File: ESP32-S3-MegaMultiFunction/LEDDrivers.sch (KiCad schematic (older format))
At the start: 21 parts, among them U701 TC4426, U702 TC4426, U703 TC4426, U704 TC4426

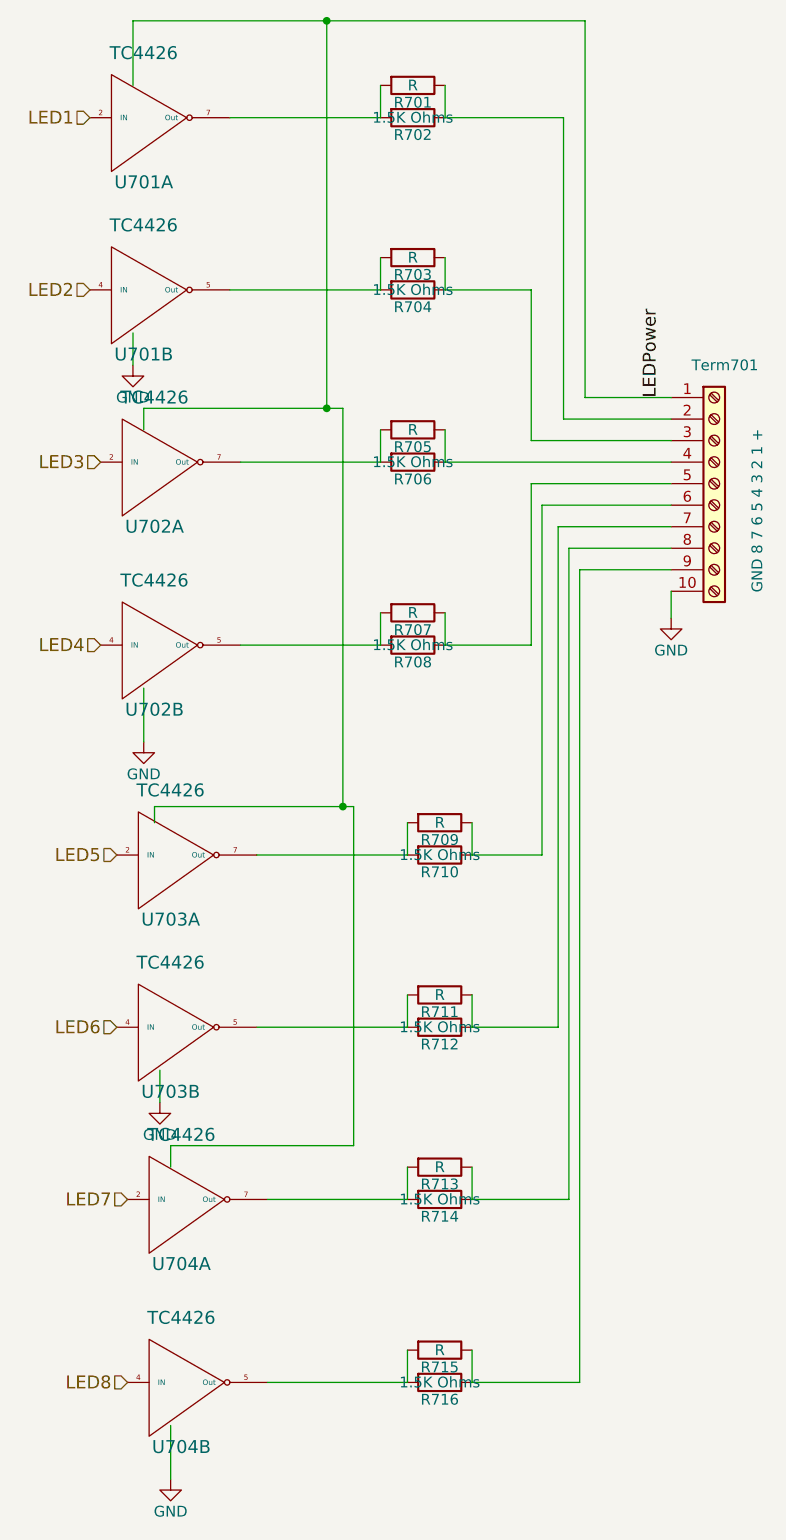
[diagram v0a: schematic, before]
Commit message: Completed ODs and LED/Drivers.
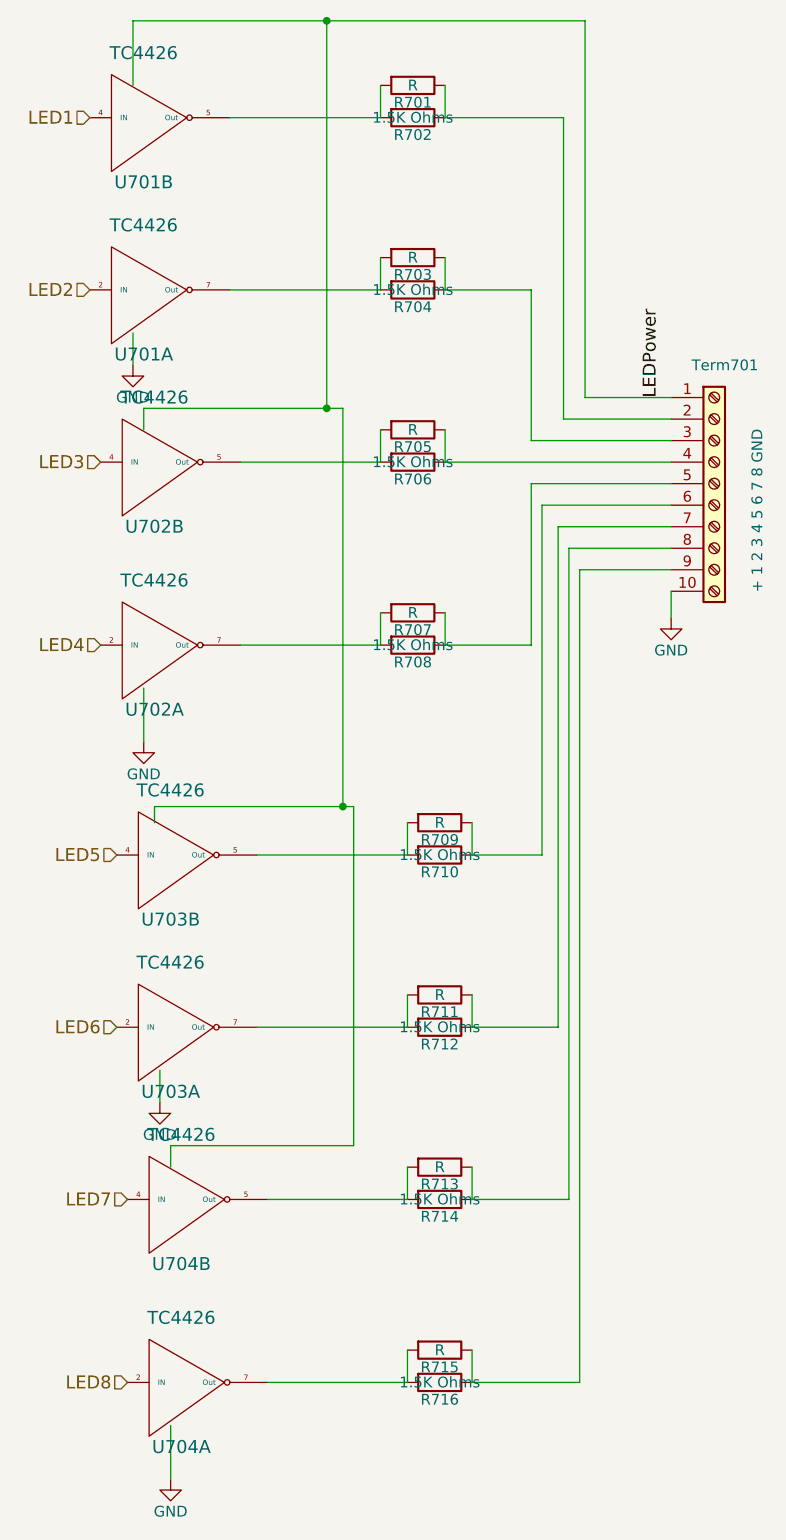
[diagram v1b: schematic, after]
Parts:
- Term701: value GND 8 7 6 5 4 3 2 1 + -> + 1 2 3 4 5 6 7 8 GND
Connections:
- net LED1: now also U701.4 (IN); no longer U701.2 (IN)
- net LED2: now also U701.2 (IN); no longer U701.4 (IN)
- net LED3: now also U702.4 (IN); no longer U702.2 (IN)
- net LED4: now also U702.2 (IN); no longer U702.4 (IN)
- net LED5: now also U703.4 (IN); no longer U703.2 (IN)
- net LED6: now also U703.2 (IN); no longer U703.4 (IN)
- net LED7: now also U704.4 (IN); no longer U704.2 (IN)
- net LED8: now also U704.2 (IN); no longer U704.4 (IN)
- net at R705.2, R706.2: now also U702.5 (Out); no longer U702.7 (Out)
- net at R707.2, R708.2: now also U702.7 (Out); no longer U702.5 (Out)
- net at R701.2, R702.2: now also U701.5 (Out); no longer U701.7 (Out)
- net at R703.2, R704.2: now also U701.7 (Out); no longer U701.5 (Out)
- net at R713.2, R714.2: now also U704.5 (Out); no longer U704.7 (Out)
- net at R715.2, R716.2: now also U704.7 (Out); no longer U704.5 (Out)
- net at R709.2, R710.2: now also U703.5 (Out); no longer U703.7 (Out)
- net at R711.2, R712.2: now also U703.7 (Out); no longer U703.5 (Out)
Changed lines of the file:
@@
 $Comp
 L TC4426 U702
-U 1 1 6346A9A9
+U 2 1 6346A9A9
 P 2625 2900
 F 0 "U702" H 2625 2600 60  0000 C CNN
@@
 F 3 "" H 2625 2900 60  0000 C CNN
 F 4 "579-TC1426COA713" H 2625 2900 60  0001 C CNN "Mouser Part Number"
-	1    2625 2900
+	2    2625 2900
 	1    0    0    -1
 $EndComp
 $Comp
 L TC4426 U702
-U 2 1 6346A9AA
+U 1 1 6346A9AA
 P 2625 3750
 F 0 "U702" H 2625 3450 60  0000 C CNN
@@
 F 3 "" H 2625 3750 60  0000 C CNN
 F 4 "579-TC1426COA713" H 2625 3750 60  0001 C CNN "Mouser Part Number"
-	2    2625 3750
+	1    2625 3750
 	1    0    0    -1
 $EndComp
@@
 P 5225 3000
 F 0 "Term701" H 5275 3550 50  0000 C CNN
-F 1 "GND 8 7 6 5 4 3 2 1 +" V 5425 2875 50  0000 C CNN
+F 1 "+ 1 2 3 4 5 6 7 8 GND" V 5425 2875 50  0000 C CNN
 F 2 "Connectors_Terminal_Blocks:TerminalBlock_Pheonix_MPT-2.54mm_10pol" H 5225 3000 50  0001 C CNN
 F 3 "" H 5225 3000 50  0001 C CNN
@@
 $Comp
 L TC4426 U701
-U 1 1 6346A9B5
+U 2 1 6346A9B5
 P 2575 1300
 F 0 "U701" H 2575 1000 60  0000 C CNN
@@
 F 3 "" H 2575 1300 60  0000 C CNN
 F 4 "579-TC1426COA713" H 2575 1300 60  0001 C CNN "Mouser Part Number"
-	1    2575 1300
+	2    2575 1300
 	1    0    0    -1
 $EndComp
 $Comp
 L TC4426 U701
-U 2 1 6346A9B6
+U 1 1 6346A9B6
 P 2575 2100
 F 0 "U701" H 2575 1800 60  0000 C CNN
@@
 F 3 "" H 2575 2100 60  0000 C CNN
 F 4 "579-TC1426COA713" H 2575 2100 60  0001 C CNN "Mouser Part Number"
-	2    2575 2100
+	1    2575 2100
 	1    0    0    -1
 $EndComp
@@
 $Comp
 L TC4426 U704
-U 1 1 6346A9B9
+U 2 1 6346A9B9
 P 2750 6325
 F 0 "U704" H 2750 6025 60  0000 C CNN
@@
 F 3 "" H 2750 6325 60  0000 C CNN
 F 4 "579-TC1426COA713" H 2750 6325 60  0001 C CNN "Mouser Part Number"
-	1    2750 6325
+	2    2750 6325
 	1    0    0    -1
 $EndComp
 $Comp
 L TC4426 U704
-U 2 1 6346A9BA
+U 1 1 6346A9BA
 P 2750 7175
 F 0 "U704" H 2750 6875 60  0000 C CNN
@@
 F 3 "" H 2750 7175 60  0000 C CNN
 F 4 "579-TC1426COA713" H 2750 7175 60  0001 C CNN "Mouser Part Number"
-	2    2750 7175
+	1    2750 7175
 	1    0    0    -1
 $EndComp
@@
 $Comp
 L TC4426 U703
-U 1 1 6346A9C3
+U 2 1 6346A9C3
 P 2700 4725
 F 0 "U703" H 2700 4425 60  0000 C CNN
@@
 F 3 "" H 2700 4725 60  0000 C CNN
 F 4 "579-TC1426COA713" H 2700 4725 60  0001 C CNN "Mouser Part Number"
-	1    2700 4725
+	2    2700 4725
 	1    0    0    -1
 $EndComp
 $Comp
 L TC4426 U703
-U 2 1 6346A9C4
+U 1 1 6346A9C4
 P 2700 5525
 F 0 "U703" H 2700 5225 60  0000 C CNN
@@
 F 3 "" H 2700 5525 60  0000 C CNN
 F 4 "579-TC1426COA713" H 2700 5525 60  0001 C CNN "Mouser Part Number"
-	2    2700 5525
-	1    0    0    -1
-$EndComp
+	1    2700 5525
+	1    0    0    -1
+$EndComp
